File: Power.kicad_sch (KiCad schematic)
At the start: 25 parts

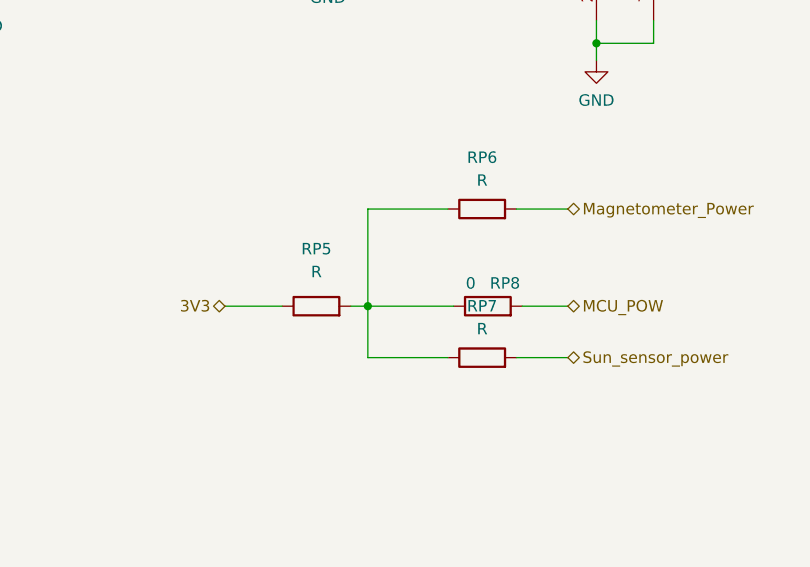
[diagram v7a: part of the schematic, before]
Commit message: Page settings changed. Added some testpoints. Some comments are made.
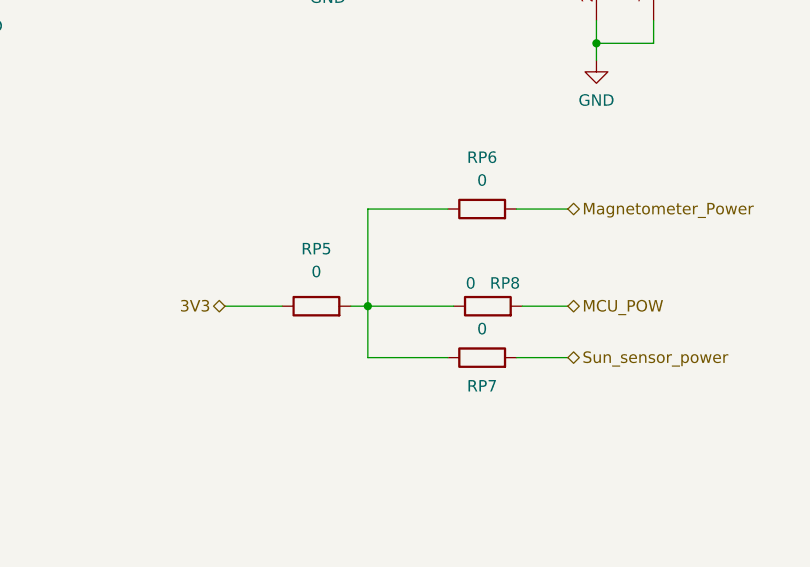
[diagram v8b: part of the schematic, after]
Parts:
- RP5, RP6, RP7: value R -> 0
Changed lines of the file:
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@@
     (in_bom yes) (on_board yes) (fields_autoplaced)
     (property "Reference" "RP6" (id 0) (at 187.325 67.31 90))
-    (property "Value" "R" (id 1) (at 187.325 69.85 90))
+    (property "Value" "0" (id 1) (at 187.325 69.85 90))
     (property "Footprint" "" (id 2) (at 187.325 74.803 90)
       (effects (font (size 1.27 1.27)) hide)
@@
   (symbol (lib_id "upsat-comms-hardware:GND") (at 200.025 56.515 0) (unit 1)
     (in_bom yes) (on_board yes) (fields_autoplaced)
-    (property "Reference" "#PWR088" (id 0) (at 200.025 62.865 0)
+    (property "Reference" "#PWR0101" (id 0) (at 200.025 62.865 0)
       (effects (font (size 1.27 1.27)) hide)
     )
@@
   )
   (symbol (lib_id "Device:R") (at 187.325 89.535 90) (unit 1)
-    (in_bom yes) (on_board yes) (fields_autoplaced)
-    (property "Reference" "RP7" (id 0) (at 187.325 83.82 90))
-    (property "Value" "R" (id 1) (at 187.325 86.36 90))
+    (in_bom yes) (on_board yes)
+    (property "Reference" "RP7" (id 0) (at 187.325 92.71 90))
+    (property "Value" "0" (id 1) (at 187.325 86.36 90))
     (property "Footprint" "" (id 2) (at 187.325 91.313 90)
       (effects (font (size 1.27 1.27)) hide)
@@
   (symbol (lib_id "upsat-comms-hardware:GND") (at 238.76 60.325 0) (unit 1)
     (in_bom yes) (on_board yes) (fields_autoplaced)
-    (property "Reference" "#PWR089" (id 0) (at 238.76 66.675 0)
+    (property "Reference" "#PWR0102" (id 0) (at 238.76 66.675 0)
       (effects (font (size 1.27 1.27)) hide)
     )
@@
   (symbol (lib_id "upsat-comms-hardware:GND") (at 119.38 148.59 0) (unit 1)
     (in_bom yes) (on_board yes) (fields_autoplaced)
-    (property "Reference" "#PWR082" (id 0) (at 119.38 154.94 0)
+    (property "Reference" "#PWR095" (id 0) (at 119.38 154.94 0)
       (effects (font (size 1.27 1.27)) hide)
     )
@@
   (symbol (lib_id "upsat-comms-hardware:GND") (at 47.625 141.605 0) (unit 1)
     (in_bom yes) (on_board yes) (fields_autoplaced)
-    (property "Reference" "#PWR076" (id 0) (at 47.625 147.955 0)
+    (property "Reference" "#PWR089" (id 0) (at 47.625 147.955 0)
       (effects (font (size 1.27 1.27)) hide)
     )
@@
   (symbol (lib_id "upsat-comms-hardware:GND") (at 170.18 45.085 0) (unit 1)
     (in_bom yes) (on_board yes) (fields_autoplaced)
-    (property "Reference" "#PWR087" (id 0) (at 170.18 51.435 0)
+    (property "Reference" "#PWR0100" (id 0) (at 170.18 51.435 0)
       (effects (font (size 1.27 1.27)) hide)
     )
@@
   (symbol (lib_id "upsat-comms-hardware:GND") (at 142.875 140.335 0) (unit 1)
     (in_bom yes) (on_board yes) (fields_autoplaced)
-    (property "Reference" "#PWR086" (id 0) (at 142.875 146.685 0)
+    (property "Reference" "#PWR099" (id 0) (at 142.875 146.685 0)
       (effects (font (size 1.27 1.27)) hide)
     )
@@
   (symbol (lib_id "power:GND") (at 81.915 57.785 0) (unit 1)
     (in_bom yes) (on_board yes) (fields_autoplaced)
-    (property "Reference" "#PWR080" (id 0) (at 81.915 64.135 0)
+    (property "Reference" "#PWR093" (id 0) (at 81.915 64.135 0)
       (effects (font (size 1.27 1.27)) hide)
     )
@@
   (symbol (lib_id "upsat-comms-hardware:GND") (at 250.19 46.99 0) (unit 1)
     (in_bom yes) (on_board yes) (fields_autoplaced)
-    (property "Reference" "#PWR090" (id 0) (at 250.19 53.34 0)
+    (property "Reference" "#PWR0103" (id 0) (at 250.19 53.34 0)
       (effects (font (size 1.27 1.27)) hide)
     )
@@
   (symbol (lib_id "upsat-comms-hardware:GND") (at 132.08 48.26 0) (unit 1)
     (in_bom yes) (on_board yes) (fields_autoplaced)
-    (property "Reference" "#PWR084" (id 0) (at 132.08 54.61 0)
+    (property "Reference" "#PWR097" (id 0) (at 132.08 54.61 0)
       (effects (font (size 1.27 1.27)) hide)
     )
@@
     (in_bom yes) (on_board yes) (fields_autoplaced)
     (property "Reference" "RP5" (id 0) (at 168.91 77.47 90))
-    (property "Value" "R" (id 1) (at 168.91 80.01 90))
+    (property "Value" "0" (id 1) (at 168.91 80.01 90))
     (property "Footprint" "" (id 2) (at 168.91 85.598 90)
       (effects (font (size 1.27 1.27)) hide)
@@
   (symbol (lib_id "upsat-comms-hardware:GND") (at 52.07 46.355 0) (unit 1)
     (in_bom yes) (on_board yes) (fields_autoplaced)
-    (property "Reference" "#PWR077" (id 0) (at 52.07 52.705 0)
+    (property "Reference" "#PWR090" (id 0) (at 52.07 52.705 0)
       (effects (font (size 1.27 1.27)) hide)
     )
@@
   (symbol (lib_id "upsat-comms-hardware:GND") (at 120.65 61.595 0) (unit 1)
     (in_bom yes) (on_board yes) (fields_autoplaced)
-    (property "Reference" "#PWR083" (id 0) (at 120.65 67.945 0)
+    (property "Reference" "#PWR096" (id 0) (at 120.65 67.945 0)
       (effects (font (size 1.27 1.27)) hide)
     )
@@
   (symbol (lib_id "upsat-comms-hardware:GND") (at 66.04 149.225 0) (unit 1)
     (in_bom yes) (on_board yes) (fields_autoplaced)
-    (property "Reference" "#PWR079" (id 0) (at 66.04 155.575 0)
+    (property "Reference" "#PWR092" (id 0) (at 66.04 155.575 0)
       (effects (font (size 1.27 1.27)) hide)
     )
@@
   (symbol (lib_id "upsat-comms-hardware:GND") (at 55.88 149.225 0) (unit 1)
     (in_bom yes) (on_board yes) (fields_autoplaced)
-    (property "Reference" "#PWR078" (id 0) (at 55.88 155.575 0)
+    (property "Reference" "#PWR091" (id 0) (at 55.88 155.575 0)
       (effects (font (size 1.27 1.27)) hide)
     )
@@
   (symbol (lib_id "upsat-comms-hardware:GND") (at 85.725 160.02 0) (unit 1)
     (in_bom yes) (on_board yes) (fields_autoplaced)
-    (property "Reference" "#PWR081" (id 0) (at 85.725 166.37 0)
+    (property "Reference" "#PWR094" (id 0) (at 85.725 166.37 0)
       (effects (font (size 1.27 1.27)) hide)
     )
@@
   (symbol (lib_id "upsat-comms-hardware:GND") (at 138.43 168.275 0) (unit 1)
     (in_bom yes) (on_board yes) (fields_autoplaced)
-    (property "Reference" "#PWR085" (id 0) (at 138.43 174.625 0)
-      (effects (font (size 1.27 1.27)) hide)
-    )
+    (property "Reference" "#PWR098" (id 0) (at 138.43 174.625 0)
+      (effects (font (size 1.27 1.27)) hide)
+    )
